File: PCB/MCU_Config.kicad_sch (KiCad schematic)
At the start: 26 parts, among them SW1 Switch

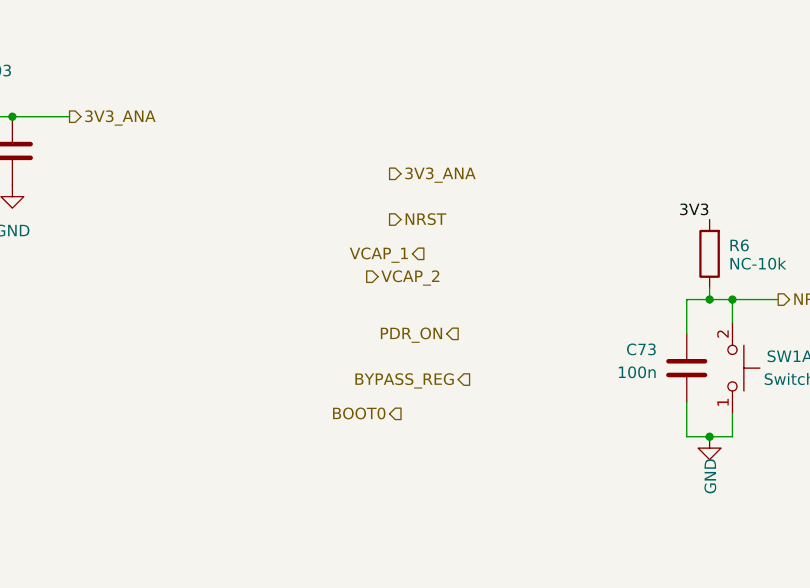
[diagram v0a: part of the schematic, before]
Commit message: Updated a lot of stuff:
Added encoders,
Added 5V power supply for actuators
Added 12V power supply for actuators
Renamed sheets to be clearer
Added usb debug
Modify MCU sheet to be A3 format
Linked some pins
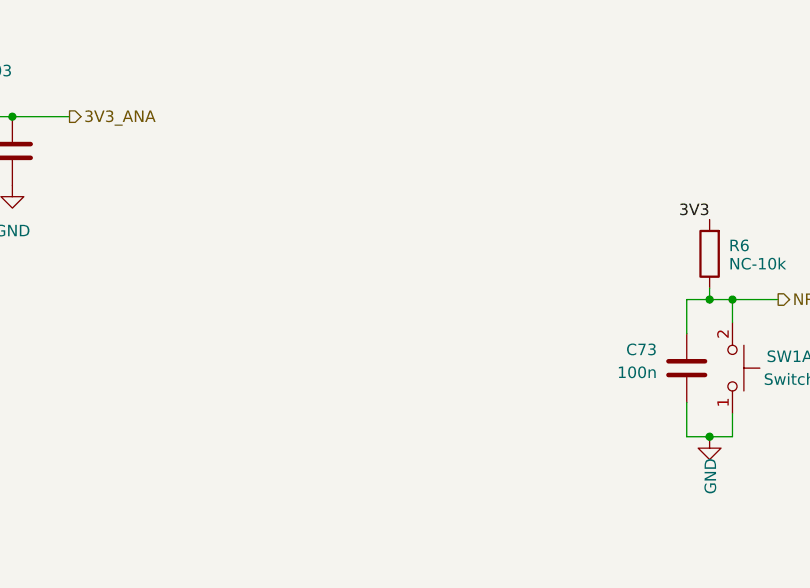
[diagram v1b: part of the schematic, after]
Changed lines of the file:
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@@
-		)
-	)
-	(hierarchical_label "PDR_ON"
-		(shape output)
-		(at 179.07 107.95 180)
-		(effects
-			(font
-				(size 1.27 1.27)
-			)
-			(justify right)
 		)
 	)
@@
 		(shape output)
 		(at 255.27 154.94 180)
-		(effects
-			(font
-				(size 1.27 1.27)
-			)
-			(justify right)
-		)
-	)
-	(hierarchical_label "VCAP_2"
-		(shape output)
-		(at 168.91 101.6 0)
-		(effects
-			(font
-				(size 1.27 1.27)
-			)
-			(justify left)
-		)
-	)
-	(hierarchical_label "BYPASS_REG"
-		(shape output)
-		(at 180.34 113.03 180)
 		(effects
 			(font
@@
 		)
 	)
-	(hierarchical_label "VCAP_1"
-		(shape output)
-		(at 175.26 99.06 180)
-		(effects
-			(font
-				(size 1.27 1.27)
-			)
-			(justify right)
-		)
-	)
-	(hierarchical_label "3V3_ANA"
-		(shape output)
-		(at 171.45 90.17 0)
-		(effects
-			(font
-				(size 1.27 1.27)
-			)
-			(justify left)
-		)
-	)
-	(hierarchical_label "BOOT0"
-		(shape output)
-		(at 172.72 116.84 180)
-		(effects
-			(font
-				(size 1.27 1.27)
-			)
-			(justify right)
-		)
-	)
-	(hierarchical_label "NRST"
-		(shape output)
-		(at 171.45 95.25 0)
-		(effects
-			(font
-				(size 1.27 1.27)
-			)
-			(justify left)
-		)
-	)
